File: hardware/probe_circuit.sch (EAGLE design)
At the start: 0 parts

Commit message: Added components to board
- added LT1920 and resistor to board
- generated PCB
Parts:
- added R1: 2.4k, eagle-ltspice:R0204/7
- added U1: LT1920CS8PBF, LTC_By_element14_Batch_1:LT1920CS8PBF
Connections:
- new net GND: U1.-VS, U1.REF
- new net RG: R1.1, U1.RG
- new net RG_2: R1.2, U1.RG_2
- new net VCC: U1.+VS
- new net VOFF: U1.-IN
- new net VPD: U1.+IN
- new net VSIG: U1.OUTPUT
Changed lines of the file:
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@@
 <grid distance="0.1" unitdist="inch" unit="inch" style="lines" multiple="1" display="no" altdistance="0.01" altunitdist="inch" altunit="inch"/>
 <layers>
+<layer number="1" name="Top" color="4" fill="1" visible="no" active="no"/>
+<layer number="16" name="Bottom" color="1" fill="1" visible="no" active="no"/>
+<layer number="17" name="Pads" color="2" fill="1" visible="no" active="no"/>
+<layer number="18" name="Vias" color="2" fill="1" visible="no" active="no"/>
+<layer number="19" name="Unrouted" color="6" fill="1" visible="no" active="no"/>
+<layer number="20" name="Dimension" color="15" fill="1" visible="no" active="no"/>
+<layer number="21" name="tPlace" color="7" fill="1" visible="no" active="no"/>
+<layer number="22" name="bPlace" color="7" fill="1" visible="no" active="no"/>
+<layer number="23" name="tOrigins" color="15" fill="1" visible="no" active="no"/>
+<layer number="24" name="bOrigins" color="15" fill="1" visible="no" active="no"/>
+<layer number="25" name="tNames" color="7" fill="1" visible="no" active="no"/>
+<layer number="26" name="bNames" color="7" fill="1" visible="no" active="no"/>
+<layer number="27" name="tValues" color="7" fill="1" visible="no" active="no"/>
+<layer number="28" name="bValues" color="7" fill="1" visible="no" active="no"/>
+<layer number="29" name="tStop" color="7" fill="3" visible="no" active="no"/>
+<layer number="30" name="bStop" color="7" fill="6" visible="no" active="no"/>
+<layer number="31" name="tCream" color="7" fill="4" visible="no" active="no"/>
+<layer number="32" name="bCream" color="7" fill="5" visible="no" active="no"/>
+<layer number="33" name="tFinish" color="6" fill="3" visible="no" active="no"/>
+<layer number="34" name="bFinish" color="6" fill="6" visible="no" active="no"/>
+<layer number="35" name="tGlue" color="7" fill="4" visible="no" active="no"/>
+<layer number="36" name="bGlue" color="7" fill="5" visible="no" active="no"/>
+<layer number="37" name="tTest" color="7" fill="1" visible="no" active="no"/>
+<layer number="38" name="bTest" color="7" fill="1" visible="no" active="no"/>
+<layer number="39" name="tKeepout" color="4" fill="11" visible="no" active="no"/>
+<layer number="40" name="bKeepout" color="1" fill="11" visible="no" active="no"/>
+<layer number="41" name="tRestrict" color="4" fill="10" visible="no" active="no"/>
+<layer number="42" name="bRestrict" color="1" fill="10" visible="no" active="no"/>
+<layer number="43" name="vRestrict" color="2" fill="10" visible="no" active="no"/>
+<layer number="44" name="Drills" color="7" fill="1" visible="no" active="no"/>
+<layer number="45" name="Holes" color="7" fill="1" visible="no" active="no"/>
+<layer number="46" name="Milling" color="3" fill="1" visible="no" active="no"/>
+<layer number="47" name="Measures" color="7" fill="1" visible="no" active="no"/>
+<layer number="48" name="Document" color="7" fill="1" visible="no" active="no"/>
+<layer number="49" name="Reference" color="7" fill="1" visible="no" active="no"/>
+<layer number="51" name="tDocu" color="7" fill="1" visible="no" active="no"/>
+<layer number="52" name="bDocu" color="7" fill="1" visible="no" active="no"/>
 <layer number="90" name="Modules" color="5" fill="1" visible="yes" active="yes"/>
 <layer number="91" name="Nets" color="2" fill="1" visible="yes" active="yes"/>
@@
 <layer number="97" name="Info" color="7" fill="1" visible="yes" active="yes"/>
 <layer number="98" name="Guide" color="6" fill="1" visible="yes" active="yes"/>
+<layer number="99" name="SpiceOrder" color="5" fill="1" visible="yes" active="yes"/>
 </layers>
 <schematic xreflabel="%F%N/%S.%C%R" xrefpart="/%S.%C%R">
@@
 </classes>
 <parts>
+<part name="U1" library="LTC_By_element14_Batch_1" deviceset="LT1920CS8PBF" device=""/>
+<part name="R1" library="eagle-ltspice" deviceset="R" device="0204/7" value="2.4k"/>
 </parts>
 <sheets>
@@
 </plain>
 <instances>
+<instance part="U1" gate="A" x="73.66" y="63.5"/>
+<instance part="R1" gate="G$1" x="20.32" y="83.82"/>
 </instances>
 <busses>
 </busses>
 <nets>
+<net name="RG_2" class="0">
+<segment>
+<pinref part="U1" gate="A" pin="RG_2"/>
+<wire x1="55.88" y1="55.88" x2="48.26" y2="55.88" width="0.1524" layer="91"/>
+<label x="48.26" y="55.88" size="1.778" layer="95"/>
+</segment>
+<segment>
+<pinref part="R1" gate="G$1" pin="2"/>
+<wire x1="25.4" y1="83.82" x2="33.02" y2="83.82" width="0.1524" layer="91"/>
+<label x="25.4" y="83.82" size="1.778" layer="95"/>
+</segment>
+</net>
+<net name="RG" class="0">
+<segment>
+<pinref part="U1" gate="A" pin="RG"/>
+<wire x1="55.88" y1="53.34" x2="48.26" y2="53.34" width="0.1524" layer="91"/>
+<label x="48.26" y="53.34" size="1.778" layer="95"/>
+</segment>
+<segment>
+<pinref part="R1" gate="G$1" pin="1"/>
+<wire x1="15.24" y1="83.82" x2="7.62" y2="83.82" width="0.1524" layer="91"/>
+<label x="7.62" y="83.82" size="1.778" layer="95"/>
+</segment>
+</net>
+<net name="VCC" class="0">
+<segment>
+<pinref part="U1" gate="A" pin="+VS"/>
+<wire x1="55.88" y1="71.12" x2="48.26" y2="71.12" width="0.1524" layer="91"/>
+<label x="48.26" y="71.12" size="1.778" layer="95"/>
+</segment>
+</net>
+<net name="VSIG" class="0">
+<segment>
+<pinref part="U1" gate="A" pin="OUTPUT"/>
+<wire x1="91.44" y1="71.12" x2="104.14" y2="71.12" width="0.1524" layer="91"/>
+<label x="91.44" y="71.12" size="1.778" layer="95"/>
+</segment>
+</net>
+<net name="VOFF" class="0">
+<segment>
+<pinref part="U1" gate="A" pin="-IN"/>
+<wire x1="55.88" y1="63.5" x2="48.26" y2="63.5" width="0.1524" layer="91"/>
+<label x="48.26" y="63.5" size="1.778" layer="95"/>
+</segment>
+</net>
+<net name="VPD" class="0">
+<segment>
+<pinref part="U1" gate="A" pin="+IN"/>
+<wire x1="55.88" y1="66.04" x2="48.26" y2="66.04" width="0.1524" layer="91"/>
+<label x="48.26" y="66.04" size="1.778" layer="95"/>
+</segment>
+</net>
+<net name="GND" class="0">
+<segment>
+<pinref part="U1" gate="A" pin="-VS"/>
+<wire x1="55.88" y1="48.26" x2="48.26" y2="48.26" width="0.1524" layer="91"/>
+<label x="48.26" y="48.26" size="1.778" layer="95"/>
+</segment>
+<segment>
+<pinref part="U1" gate="A" pin="REF"/>
+<wire x1="55.88" y1="58.42" x2="48.26" y2="58.42" width="0.1524" layer="91"/>
+<label x="48.26" y="58.42" size="1.778" layer="95"/>
+</segment>
+</net>
 </nets>
 </sheet>

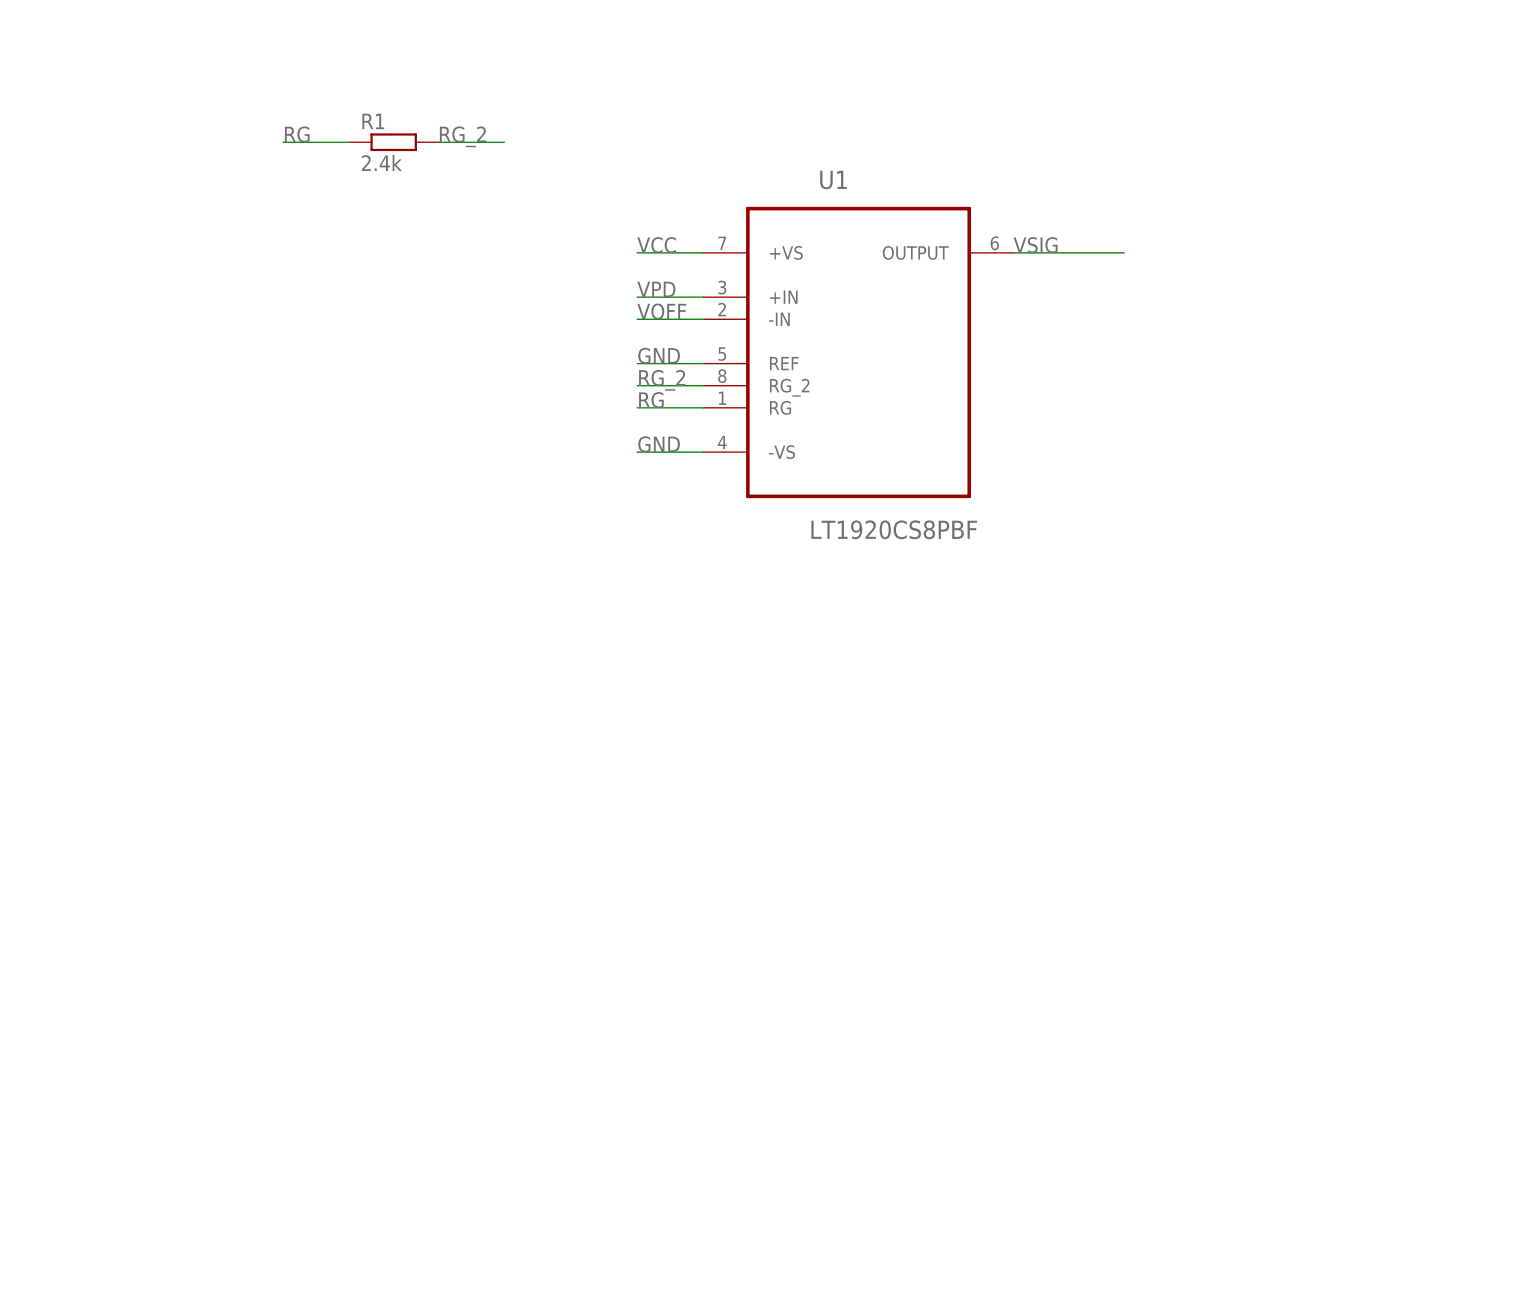
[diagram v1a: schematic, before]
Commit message: - updated PCB
- added example switches, connector points and resistors to the board
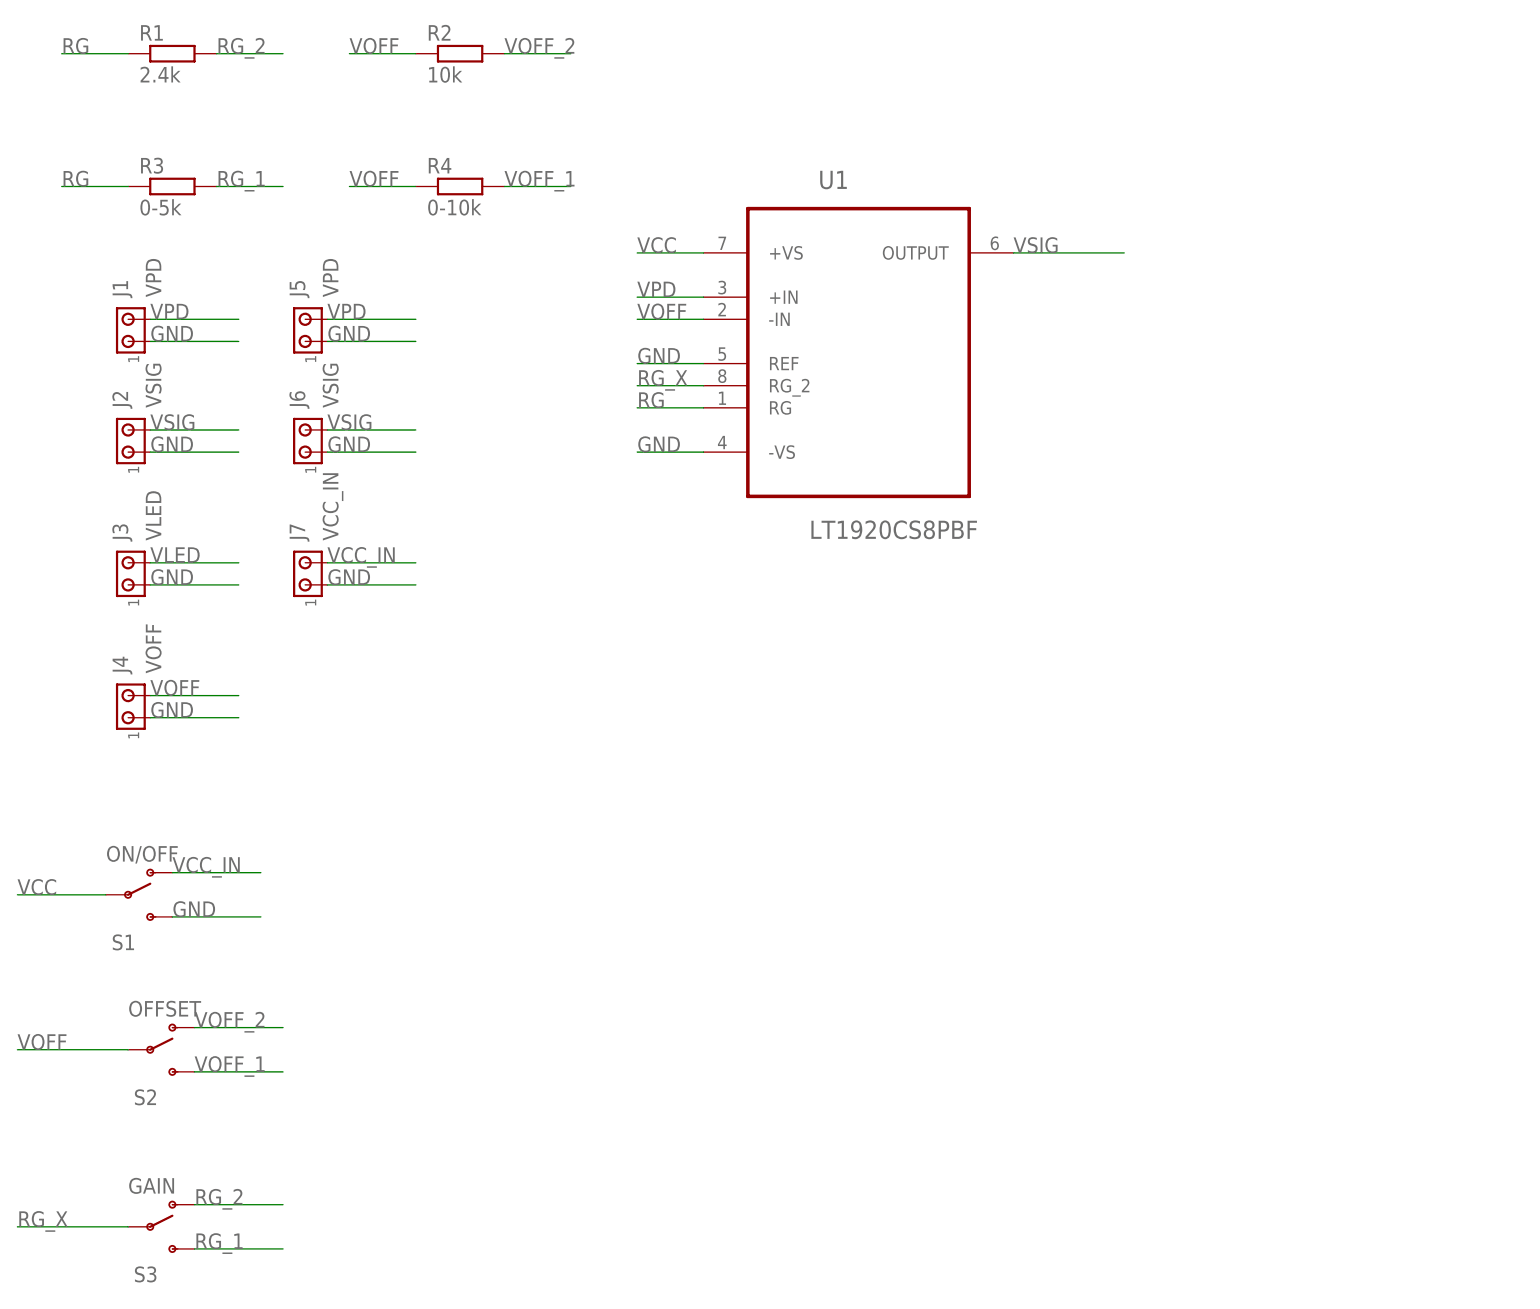
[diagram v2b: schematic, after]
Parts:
- added J1, J5: VPD, con-amp:MTA02-100
- added J2, J6: VSIG, con-amp:MTA02-100
- added J3: VLED, con-amp:MTA02-100
- added J4: VOFF, con-amp:MTA02-100
- added J7: VCC_IN, con-amp:MTA02-100
- added R2: 10k, eagle-ltspice:R0204/7
- added R3: 0-5k, eagle-ltspice:R0204/7
- added R4: 0-10k, eagle-ltspice:R0204/7
- added S1: ON/OFF, SparkFun-Electromechanical:SWITCH-SPDTPTH
- added S2: OFFSET, SparkFun-Electromechanical:SWITCH-SPDTPTH
- added S3: GAIN, SparkFun-Electromechanical:SWITCH-SPDTPTH
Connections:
- new net RG_1: R3.2, S3.S
- new net RG_X: S3.P, U1.RG_2
- new net VCC_IN: J7.2, S1.O
- new net VLED: J3.2
- new net VOFF_1: R4.2, S2.S
- new net VOFF_2: R2.2, S2.O
- net GND: now also J1.1, J2.1, J3.1, J4.1, J5.1, J6.1, J7.1, S1.S
- net RG: now also R3.1
- net RG_2: now also S3.O; no longer U1.RG_2
- net VCC: now also S1.P
- net VOFF: now also J4.2, R2.1, R4.1, S2.P
- net VPD: now also J1.2, J5.2
- net VSIG: now also J2.2, J6.2
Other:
- moved on the sheet: R1
